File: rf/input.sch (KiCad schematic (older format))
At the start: 13 parts, among them U601 MGA-645T6, U602 MGA-645T6

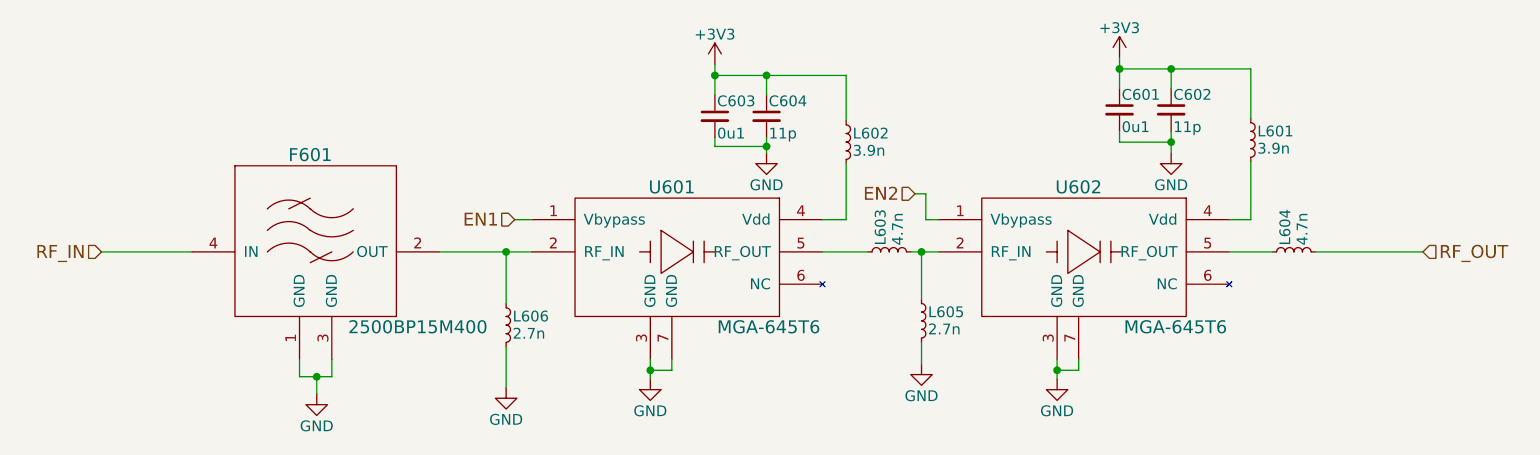
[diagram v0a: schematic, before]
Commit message: Finish assigning component footprints
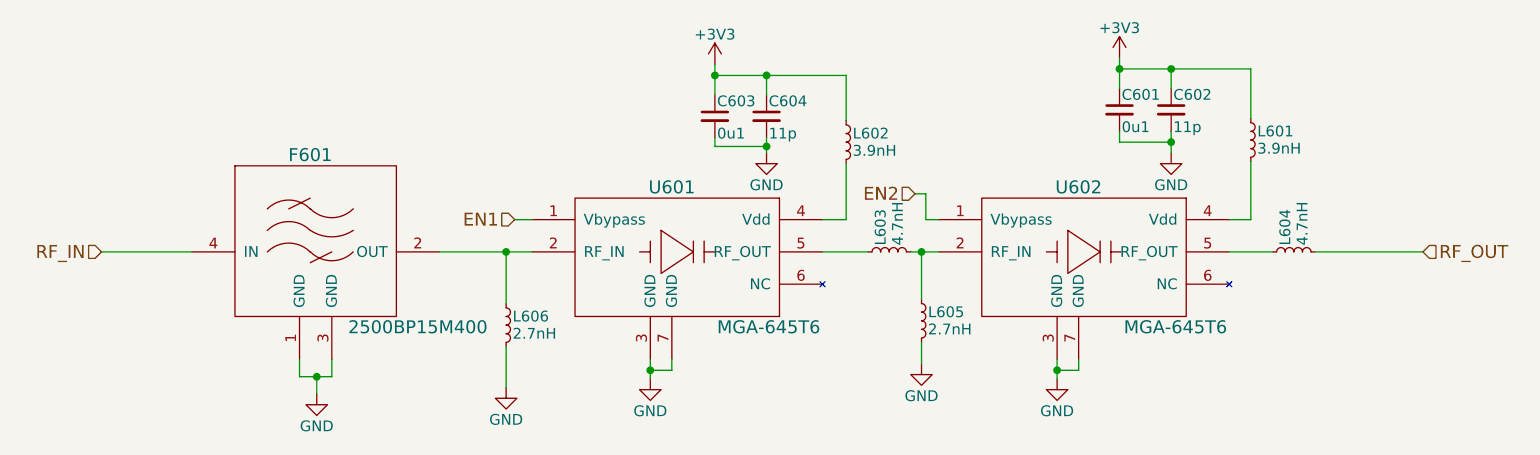
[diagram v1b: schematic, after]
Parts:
- L601, L602: value 3.9n -> 3.9nH
- L603, L604: value 4.7n -> 4.7nH
- L605, L606: value 2.7n -> 2.7nH
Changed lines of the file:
@@
 $EndComp
 $Comp
-L GND #PWR057
+L GND #PWR509
 U 1 1 59D64760
 P 3360 4390
-F 0 "#PWR057" H 3360 4140 50  0001 C CNN
+F 0 "#PWR509" H 3360 4140 50  0001 C CNN
 F 1 "GND" H 3360 4240 50  0000 C CNN
 F 2 "" H 3360 4390 50  0001 C CNN
@@
 $EndComp
 $Comp
-L GND #PWR058
+L GND #PWR506
 U 1 1 59D653F1
 P 4910 4320
-F 0 "#PWR058" H 4910 4070 50  0001 C CNN
+F 0 "#PWR506" H 4910 4070 50  0001 C CNN
 F 1 "GND" H 4910 4170 50  0000 C CNN
 F 2 "" H 4910 4320 50  0001 C CNN
@@
 $EndComp
 $Comp
-L GND #PWR059
+L GND #PWR507
 U 1 1 59D659C2
 P 6800 4320
-F 0 "#PWR059" H 6800 4070 50  0001 C CNN
+F 0 "#PWR507" H 6800 4070 50  0001 C CNN
 F 1 "GND" H 6800 4170 50  0000 C CNN
 F 2 "" H 6800 4320 50  0001 C CNN
@@
 P 4240 4070
 F 0 "L606" H 4270 4110 50  0000 L CNN
-F 1 "2.7n" H 4270 4030 50  0000 L CNN
+F 1 "2.7nH" H 4270 4030 50  0000 L CNN
 F 2 "Capacitors_SMD:C_0402" H 4240 4070 50  0001 C CNN
 F 3 "" H 4240 4070 50  0001 C CNN
@@
 P 6170 4050
 F 0 "L605" H 6200 4090 50  0000 L CNN
-F 1 "2.7n" H 6200 4010 50  0000 L CNN
+F 1 "2.7nH" H 6200 4010 50  0000 L CNN
 F 2 "Capacitors_SMD:C_0402" H 6170 4050 50  0001 C CNN
 F 3 "" H 6170 4050 50  0001 C CNN
@@
 P 6020 3730
 F 0 "L603" H 6050 3770 50  0000 L CNN
-F 1 "4.7n" H 6050 3690 50  0000 L CNN
+F 1 "4.7nH" H 6050 3690 50  0000 L CNN
 F 2 "Capacitors_SMD:C_0402" H 6020 3730 50  0001 C CNN
 F 3 "" H 6020 3730 50  0001 C CNN
@@
 P 7900 3730
 F 0 "L604" H 7930 3770 50  0000 L CNN
-F 1 "4.7n" H 7930 3690 50  0000 L CNN
+F 1 "4.7nH" H 7930 3690 50  0000 L CNN
 F 2 "Capacitors_SMD:C_0402" H 7900 3730 50  0001 C CNN
 F 3 "" H 7900 3730 50  0001 C CNN
@@
 Connection ~ 4240 3730
 $Comp
-L GND #PWR060
+L GND #PWR508
 U 1 1 59D67ABC
 P 4240 4360
-F 0 "#PWR060" H 4240 4110 50  0001 C CNN
+F 0 "#PWR508" H 4240 4110 50  0001 C CNN
 F 1 "GND" H 4240 4210 50  0000 C CNN
 F 2 "" H 4240 4360 50  0001 C CNN
@@
 	4240 4360 4240 4170
 $Comp
-L GND #PWR061
+L GND #PWR505
 U 1 1 59D67C59
 P 6170 4250
-F 0 "#PWR061" H 6170 4000 50  0001 C CNN
+F 0 "#PWR505" H 6170 4000 50  0001 C CNN
 F 1 "GND" H 6170 4100 50  0000 C CNN
 F 2 "" H 6170 4250 50  0001 C CNN
@@
 	6170 4150 6170 4250
 $Comp
-L +3V3 #PWR062
+L +3V3 #PWR502
 U 1 1 59D67FA5
 P 5210 2860
-F 0 "#PWR062" H 5210 2710 50  0001 C CNN
+F 0 "#PWR502" H 5210 2710 50  0001 C CNN
 F 1 "+3V3" H 5210 3000 50  0000 C CNN
 F 2 "" H 5210 2860 50  0001 C CNN
@@
 P 5820 3220
 F 0 "L602" H 5850 3260 50  0000 L CNN
-F 1 "3.9n" H 5850 3180 50  0000 L CNN
+F 1 "3.9nH" H 5850 3180 50  0000 L CNN
 F 2 "Capacitors_SMD:C_0402" H 5820 3220 50  0001 C CNN
 F 3 "" H 5820 3220 50  0001 C CNN
@@
 P 7700 3210
 F 0 "L601" H 7730 3250 50  0000 L CNN
-F 1 "3.9n" H 7730 3170 50  0000 L CNN
+F 1 "3.9nH" H 7730 3170 50  0000 L CNN
 F 2 "Capacitors_SMD:C_0402" H 7700 3210 50  0001 C CNN
 F 3 "" H 7700 3210 50  0001 C CNN
@@
 Connection ~ 5210 2910
 $Comp
-L +3V3 #PWR063
+L +3V3 #PWR501
 U 1 1 59D6867B
 P 7090 2830
-F 0 "#PWR063" H 7090 2680 50  0001 C CNN
+F 0 "#PWR501" H 7090 2680 50  0001 C CNN
 F 1 "+3V3" H 7090 2970 50  0000 C CNN
 F 2 "" H 7090 2830 50  0001 C CNN
@@
 Connection ~ 5450 2910
 $Comp
-L GND #PWR064
+L GND #PWR503
 U 1 1 59D6874C
 P 5450 3270
-F 0 "#PWR064" H 5450 3020 50  0001 C CNN
+F 0 "#PWR503" H 5450 3020 50  0001 C CNN
 F 1 "GND" H 5450 3120 50  0000 C CNN
 F 2 "" H 5450 3270 50  0001 C CNN
@@
 $EndComp
 $Comp
-L GND #PWR065
+L GND #PWR504
 U 1 1 59D6878B
 P 7330 3270
-F 0 "#PWR065" H 7330 3020 50  0001 C CNN
+F 0 "#PWR504" H 7330 3020 50  0001 C CNN
 F 1 "GND" H 7330 3120 50  0000 C CNN
 F 2 "" H 7330 3270 50  0001 C CNN

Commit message: Finish first revision layout
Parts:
- renumbered C601 to C501, C602 to C502, C603 to C503, C604 to C504, F601 to F501, L601 to L501, L602 to L502, L603 to L503, L604 to L504, L605 to L505, L606 to L506, U601 to U501, U602 to U502
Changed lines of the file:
@@
 LIBS:mc2016k30
 LIBS:cp0402q5425entr
+LIBS:lm340-5
 EELAYER 25 0
 EELAYER END
@@
 $EndDescr
 $Comp
-L 2500BP15M400 F601
+L 2500BP15M400 F501
 U 1 1 59D64427
 P 3330 3730
-F 0 "F601" H 3330 4180 60  0000 C CNN
+F 0 "F501" H 3330 4180 60  0000 C CNN
 F 1 "2500BP15M400" H 3830 3380 60  0000 C CNN
 F 2 "rajsradar:2500BP15M400" H 3330 3730 60  0001 C CNN
@@
 $EndComp
 $Comp
-L MGA-645T6 U601
+L MGA-645T6 U501
 U 1 1 59D64DB0
 P 5010 3730
-F 0 "U601" H 5010 4030 60  0000 C CNN
+F 0 "U501" H 5010 4030 60  0000 C CNN
 F 1 "MGA-645T6" H 5460 3380 60  0000 C CNN
 F 2 "rajsradar:MGA-645T6" H 5010 3730 60  0001 C CNN
@@
 $EndComp
 $Comp
-L MGA-645T6 U602
+L MGA-645T6 U502
 U 1 1 59D659BC
 P 6900 3730
-F 0 "U602" H 6900 4030 60  0000 C CNN
+F 0 "U502" H 6900 4030 60  0000 C CNN
 F 1 "MGA-645T6" H 7350 3380 60  0000 C CNN
 F 2 "rajsradar:MGA-645T6" H 6900 3730 60  0001 C CNN
@@
 RF_OUT
 $Comp
-L L_Small L606
+L L_Small L506
 U 1 1 59D6720C
 P 4240 4070
-F 0 "L606" H 4270 4110 50  0000 L CNN
+F 0 "L506" H 4270 4110 50  0000 L CNN
 F 1 "2.7nH" H 4270 4030 50  0000 L CNN
 F 2 "Capacitors_SMD:C_0402" H 4240 4070 50  0001 C CNN
@@
 	2360 3730 2780 3730
 $Comp
-L L_Small L605
+L L_Small L505
 U 1 1 59D673E1
 P 6170 4050
-F 0 "L605" H 6200 4090 50  0000 L CNN
+F 0 "L505" H 6200 4090 50  0000 L CNN
 F 1 "2.7nH" H 6200 4010 50  0000 L CNN
 F 2 "Capacitors_SMD:C_0402" H 6170 4050 50  0001 C CNN
@@
 $EndComp
 $Comp
-L L_Small L603
+L L_Small L503
 U 1 1 59D67473
 P 6020 3730
-F 0 "L603" H 6050 3770 50  0000 L CNN
+F 0 "L503" H 6050 3770 50  0000 L CNN
 F 1 "4.7nH" H 6050 3690 50  0000 L CNN
 F 2 "Capacitors_SMD:C_0402" H 6020 3730 50  0001 C CNN
@@
 $EndComp
 $Comp
-L L_Small L604
+L L_Small L504
 U 1 1 59D67614
 P 7900 3730
-F 0 "L604" H 7930 3770 50  0000 L CNN
+F 0 "L504" H 7930 3770 50  0000 L CNN
 F 1 "4.7nH" H 7930 3690 50  0000 L CNN
 F 2 "Capacitors_SMD:C_0402" H 7900 3730 50  0001 C CNN
@@
 $EndComp
 $Comp
-L L_Small L602
+L L_Small L502
 U 1 1 59D67FDD
 P 5820 3220
-F 0 "L602" H 5850 3260 50  0000 L CNN
+F 0 "L502" H 5850 3260 50  0000 L CNN
 F 1 "3.9nH" H 5850 3180 50  0000 L CNN
 F 2 "Capacitors_SMD:C_0402" H 5820 3220 50  0001 C CNN
@@
 $EndComp
 $Comp
-L L_Small L601
+L L_Small L501
 U 1 1 59D680B8
 P 7700 3210
-F 0 "L601" H 7730 3250 50  0000 L CNN
+F 0 "L501" H 7730 3250 50  0000 L CNN
 F 1 "3.9nH" H 7730 3170 50  0000 L CNN
 F 2 "Capacitors_SMD:C_0402" H 7700 3210 50  0001 C CNN
@@
 	7700 3580 7700 3310
 $Comp
-L C_Small C604
+L C_Small C504
 U 1 1 59D6822A
 P 5450 3100
-F 0 "C604" H 5460 3170 50  0000 L CNN
+F 0 "C504" H 5460 3170 50  0000 L CNN
 F 1 "11p" H 5460 3020 50  0000 L CNN
 F 2 "Capacitors_SMD:C_0402" H 5450 3100 50  0001 C CNN
@@
 $EndComp
 $Comp
-L C_Small C603
+L C_Small C503
 U 1 1 59D68289
 P 5210 3100
-F 0 "C603" H 5220 3170 50  0000 L CNN
+F 0 "C503" H 5220 3170 50  0000 L CNN
 F 1 "0u1" H 5220 3020 50  0000 L CNN
 F 2 "Capacitors_SMD:C_0603_HandSoldering" H 5210 3100 50  0001 C CNN
@@
 $EndComp
 $Comp
-L C_Small C602
+L C_Small C502
 U 1 1 59D68681
 P 7330 3070
-F 0 "C602" H 7340 3140 50  0000 L CNN
+F 0 "C502" H 7340 3140 50  0000 L CNN
 F 1 "11p" H 7340 2990 50  0000 L CNN
 F 2 "Capacitors_SMD:C_0402" H 7330 3070 50  0001 C CNN
@@
 $EndComp
 $Comp
-L C_Small C601
+L C_Small C501
 U 1 1 59D68687
 P 7090 3070
-F 0 "C601" H 7100 3140 50  0000 L CNN
+F 0 "C501" H 7100 3140 50  0000 L CNN
 F 1 "0u1" H 7100 2990 50  0000 L CNN
 F 2 "Capacitors_SMD:C_0603_HandSoldering" H 7090 3070 50  0001 C CNN
